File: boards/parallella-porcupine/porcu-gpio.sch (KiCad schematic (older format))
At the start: 4 parts, among them J1 CONN\\HDR\\P1\\1R02, J2 CONN\\HDR\\P1\\1R02, J3 CONN\\HDR\\P1\\2R15\\SHD, J4 CONN\\HDR\\P1\\2R15\\SHD

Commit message: Schematic is stable, PCB mostly routed.
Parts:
- removed J3, J4: CONN\\HDR\\P1\\2R15\\SHD, CONN_HDR_P1_2R15_SHD, symbol CONN\HDR\P1\2R15\SHD
- added J3: CONN\\HDR\\P1FRA\\2R06, CONN_HDR_P1FRA_2R06, symbol CONN\HDR\P1FRA\2R06
- added J4, J5: CONN\\HDR\\P1\\2R15, CONN_HDR_P1_2R15, symbol CONN\HDR\P1\2R15
- added R1, R2, R3, R4, R5, R6, R7, R8: 200, R_0805_HS, symbol R\SMD0805\1PCT\200
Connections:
- net labels added: 3P3V, PMOD11, PMOD12, PMOD13, PMOD14, PMOD21, PMOD22, PMOD23, PMOD24
- wire segments 70 -> 92
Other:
- note added: "1 -- 6"
- note added: "11\n1\n\n7\n12"
- note added: "1\n6\n\n12\n2"
- note added: "3\n5\n\n11\n4"
- note added: "5\n4\n\n10\n6"
- note added: "7 -- 12"
- note added: "7\n3\n\n9\n8"
- note added: "9\n2\n\n8\n10"
- note added: "NOTE: Pin numbering for PMODs is \nnon-standard. The numbering \nlooking into the host (female) connector:"
- note added: "PMOD Connector"
- note added: "Place series Rs to minimize\nstubs on differential GPIO_P/N."
- note added: "STD\nPMOD\n\nPMOD\nSTD"
- moved on the sheet: J1, J2

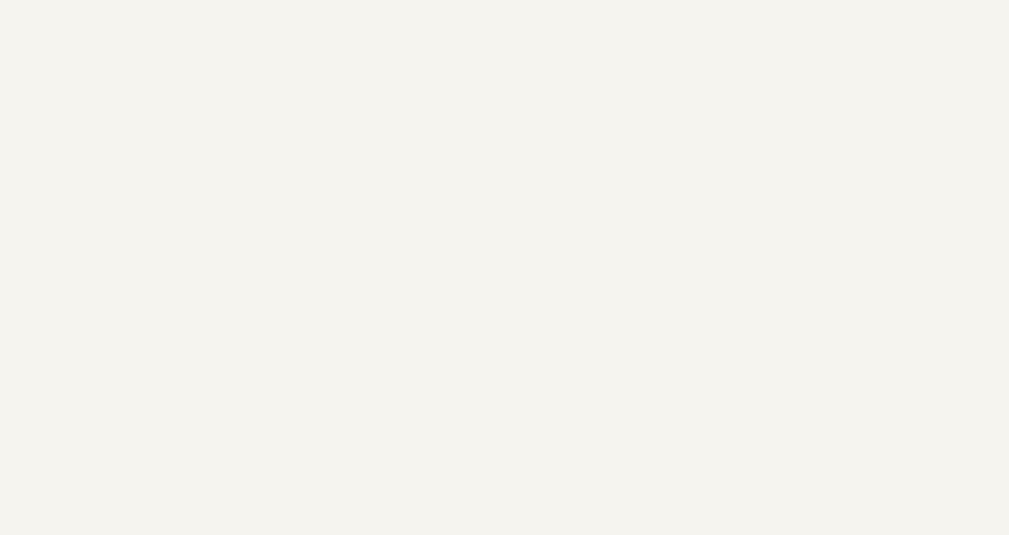
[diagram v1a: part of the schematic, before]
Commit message: Completed design w/3-row XID/YID and various 4-pin IO connectors. Fixed page ordering, changed "Mfr" field to "Manufacturer" Will now re-do to combine all misc. functions onto a single 2xN connector.
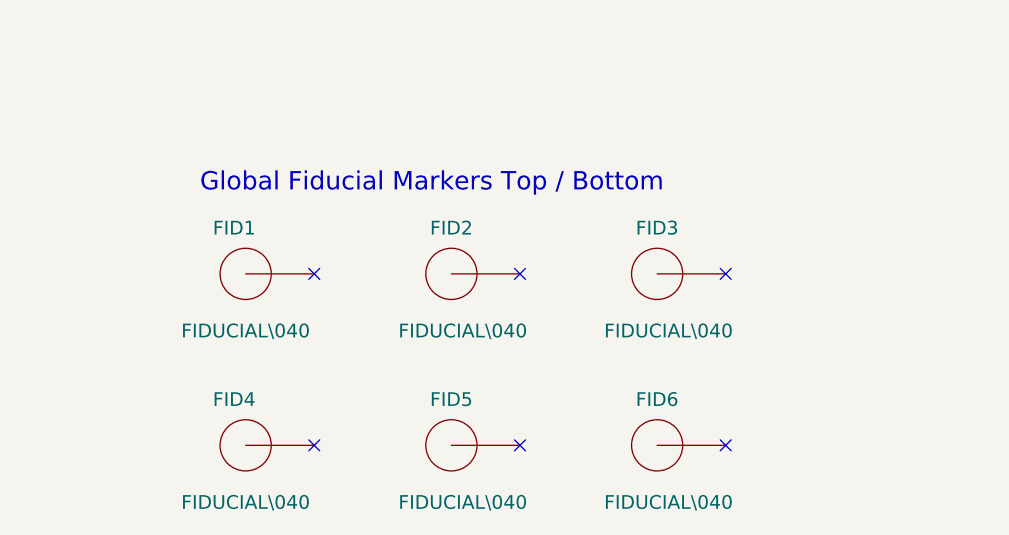
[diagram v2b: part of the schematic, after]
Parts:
- added FID1, FID2, FID3, FID4, FID5, FID6: FIDUCIAL\\040, FIDUCIAL_040, symbol FIDUCIAL\040
- J1, J2: MFR 3M -> (none); Manufacturer (none) -> 3M
- J3, J4, J5: MFR Sullins -> (none); Manufacturer (none) -> Sullins
- R1, R2, R3, R4, R5, R6, R7, R8: MFR Yageo -> (none); Manufacturer (none) -> Yageo
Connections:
- no-connect marks 0 -> 6
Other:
- note added: "Global Fiducial Markers Top / Bottom"
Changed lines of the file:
@@
 $Descr B 17000 11000
 encoding utf-8
-Sheet 6 10
+Sheet 8 10
 Title "Parallella Breakout Daughtercard"
 Date "09 May 2014"
@@
 GPIO_P23
 $Comp
-L GND #PWR010
+L GND #PWR021
 U 1 1 538C694D
 P 9250 4750
-F 0 "#PWR010" H 9250 4750 30  0001 C CNN
+F 0 "#PWR021" H 9250 4750 30  0001 C CNN
 F 1 "GND" H 9250 4680 30  0001 C CNN
 F 2 "" H 9250 4750 60  0000 C CNN
@@
 $EndComp
 $Comp
-L GND #PWR011
+L GND #PWR022
 U 1 1 538C6961
 P 11550 4750
-F 0 "#PWR011" H 11550 4750 30  0001 C CNN
+F 0 "#PWR022" H 11550 4750 30  0001 C CNN
 F 1 "GND" H 11550 4680 30  0001 C CNN
 F 2 "" H 11550 4750 60  0000 C CNN
@@
 $EndComp
 $Comp
-L GND #PWR012
+L GND #PWR023
 U 1 1 538C6975
 P 9250 7700
-F 0 "#PWR012" H 9250 7700 30  0001 C CNN
+F 0 "#PWR023" H 9250 7700 30  0001 C CNN
 F 1 "GND" H 9250 7630 30  0001 C CNN
 F 2 "" H 9250 7700 60  0000 C CNN
@@
 $EndComp
 $Comp
-L GND #PWR013
+L GND #PWR024
 U 1 1 538C6989
 P 11550 7650
-F 0 "#PWR013" H 11550 7650 30  0001 C CNN
+F 0 "#PWR024" H 11550 7650 30  0001 C CNN
 F 1 "GND" H 11550 7580 30  0001 C CNN
 F 2 "" H 11550 7650 60  0000 C CNN
@@
 GPIO_P[0..23]
 $Comp
-L GND #PWR014
+L GND #PWR025
 U 1 1 538C747F
 P 5600 3100
-F 0 "#PWR014" H 5600 3100 30  0001 C CNN
+F 0 "#PWR025" H 5600 3100 30  0001 C CNN
 F 1 "GND" H 5600 3030 30  0001 C CNN
 F 2 "" H 5600 3100 60  0000 C CNN
@@
 F 3 "" H 5050 2750 60  0001 C CNN
 F 4 "961102-6404-AR" H 5200 2700 50  0000 C CNN "MFRPN"
-F 5 "3M" H 5050 2900 50  0001 C CNN "MFR"
+F 5 "3M" H 5050 2900 50  0001 C CNN "Manufacturer"
 	1    5050 2550
 	1    0    0    -1
@@
 F 3 "" H 5050 3150 60  0001 C CNN
 F 4 "961102-6404-AR" H 5200 3100 50  0000 C CNN "MFRPN"
-F 5 "3M" H 5050 3300 50  0001 C CNN "MFR"
+F 5 "3M" H 5050 3300 50  0001 C CNN "Manufacturer"
 	1    5050 2950
 	1    0    0    -1
@@
 F 3 "" V 6330 5500 30  0000 C CNN
 F 4 "RC0805FR-07200RL" V 6340 5520 60  0001 C CNN "MFRPN"
-F 5 "Yageo" V 6450 5500 60  0001 C CNN "MFR"
+F 5 "Yageo" V 6450 5500 60  0001 C CNN "Manufacturer"
 	1    6250 5500
 	0    -1   -1   0
@@
 F 3 "" H 5050 5800 60  0001 C CNN
 F 4 "PPPC062LJBN-RC" H 5200 5750 50  0000 C CNN "MFRPN"
-F 5 "Sullins" H 5100 5950 50  0001 C CNN "MFR"
+F 5 "Sullins" H 5100 5950 50  0001 C CNN "Manufacturer"
 	1    5100 5350
 	1    0    0    -1
 $EndComp
 $Comp
-L GND #PWR015
+L GND #PWR026
 U 1 1 5397567C
 P 4700 5750
-F 0 "#PWR015" H 4700 5750 30  0001 C CNN
+F 0 "#PWR026" H 4700 5750 30  0001 C CNN
 F 1 "GND" H 4700 5680 30  0001 C CNN
 F 2 "" H 4700 5750 60  0000 C CNN
@@
 $EndComp
 $Comp
-L GND #PWR016
+L GND #PWR027
 U 1 1 53975690
 P 5500 5750
-F 0 "#PWR016" H 5500 5750 30  0001 C CNN
+F 0 "#PWR027" H 5500 5750 30  0001 C CNN
 F 1 "GND" H 5500 5680 30  0001 C CNN
 F 2 "" H 5500 5750 60  0000 C CNN
@@
 F 3 "" V 6330 5600 30  0000 C CNN
 F 4 "RC0805FR-07200RL" V 6100 5500 60  0000 C CNN "MFRPN"
-F 5 "Yageo" V 6450 5600 60  0001 C CNN "MFR"
+F 5 "Yageo" V 6450 5600 60  0001 C CNN "Manufacturer"
 	1    6250 5600
 	0    -1   -1   0
@@
 F 3 "" H 10400 4950 60  0001 C CNN
 F 4 "PRPC015DAAN-RC" H 10550 4900 50  0000 C CNN "MFRPN"
-F 5 "Sullins" H 10400 5100 50  0001 C CNN "MFR"
+F 5 "Sullins" H 10400 5100 50  0001 C CNN "Manufacturer"
 	1    10400 4050
 	1    0    0    -1
@@
 F 3 "" H 10400 7850 60  0001 C CNN
 F 4 "PRPC015DAAN-RC" H 10550 7800 50  0000 C CNN "MFRPN"
-F 5 "Sullins" H 10400 8000 50  0001 C CNN "MFR"
+F 5 "Sullins" H 10400 8000 50  0001 C CNN "Manufacturer"
 	1    10400 6950
 	1    0    0    -1
@@
 F 3 "" V 6330 5400 30  0000 C CNN
 F 4 "RC0805FR-07200RL" V 6340 5420 60  0001 C CNN "MFRPN"
-F 5 "Yageo" V 6450 5400 60  0001 C CNN "MFR"
+F 5 "Yageo" V 6450 5400 60  0001 C CNN "Manufacturer"
 	1    6250 5400
 	0    -1   -1   0
@@
 F 3 "" V 6330 5300 30  0000 C CNN
 F 4 "RC0805FR-07200RL" V 6340 5320 60  0001 C CNN "MFRPN"
-F 5 "Yageo" V 6450 5300 60  0001 C CNN "MFR"
+F 5 "Yageo" V 6450 5300 60  0001 C CNN "Manufacturer"
 	1    6250 5300
 	0    -1   -1   0
@@
 F 3 "" V 4030 5500 30  0000 C CNN
 F 4 "RC0805FR-07200RL" V 4040 5520 60  0001 C CNN "MFRPN"
-F 5 "Yageo" V 4150 5500 60  0001 C CNN "MFR"
+F 5 "Yageo" V 4150 5500 60  0001 C CNN "Manufacturer"
 	1    3950 5500
 	0    -1   -1   0
@@
 F 3 "" V 4030 5600 30  0000 C CNN
 F 4 "RC0805FR-07200RL" V 3800 5500 60  0001 C CNN "MFRPN"
-F 5 "Yageo" V 4150 5600 60  0001 C CNN "MFR"
+F 5 "Yageo" V 4150 5600 60  0001 C CNN "Manufacturer"
 	1    3950 5600
 	0    -1   -1   0
@@
 F 3 "" V 4030 5400 30  0000 C CNN
 F 4 "RC0805FR-07200RL" V 4040 5420 60  0001 C CNN "MFRPN"
-F 5 "Yageo" V 4150 5400 60  0001 C CNN "MFR"
+F 5 "Yageo" V 4150 5400 60  0001 C CNN "Manufacturer"
 	1    3950 5400
 	0    -1   -1   0
@@
 F 3 "" V 4030 5300 30  0000 C CNN
 F 4 "RC0805FR-07200RL" V 4040 5320 60  0001 C CNN "MFRPN"
-F 5 "Yageo" V 4150 5300 60  0001 C CNN "MFR"
+F 5 "Yageo" V 4150 5300 60  0001 C CNN "Manufacturer"
 	1    3950 5300
 	0    -1   -1   0
 $EndComp
+$Comp
+L FIDUCIAL\040 FID1
+U 1 1 539F4400
+P 7850 9050
+F 0 "FID1" H 7800 9250 60  0000 C CNN
+F 1 "FIDUCIAL\\040" H 7850 8800 60  0000 C CNN
+F 2 "FIDUCIAL_040" H 7850 9800 60  0001 C CNN
+F 3 "N/A" H 7850 9450 60  0001 C CNN
+F 4 "N/A" H 7850 9700 80  0001 C CNN "MFRPN"
+F 5 "N/A" H 7850 9550 60  0001 C CNN "Manufacturer"
+	1    7850 9050
+	1    0    0    -1
+$EndComp
+$Comp
+L FIDUCIAL\040 FID2
+U 1 1 539F4422
+P 8750 9050
+F 0 "FID2" H 8750 9250 60  0000 C CNN
+F 1 "FIDUCIAL\\040" H 8800 8800 60  0000 C CNN
+F 2 "FIDUCIAL_040" H 8750 9800 60  0001 C CNN
+F 3 "N/A" H 8750 9450 60  0001 C CNN
+F 4 "N/A" H 8750 9700 80  0001 C CNN "MFRPN"
+F 5 "N/A" H 8750 9550 60  0001 C CNN "Manufacturer"
+	1    8750 9050
+	1    0    0    -1
+$EndComp
+$Comp
+L FIDUCIAL\040 FID3
+U 1 1 539F4444
+P 9650 9050
+F 0 "FID3" H 9650 9250 60  0000 C CNN
+F 1 "FIDUCIAL\\040" H 9700 8800 60  0000 C CNN
+F 2 "FIDUCIAL_040" H 9650 9800 60  0001 C CNN
+F 3 "N/A" H 9650 9450 60  0001 C CNN
+F 4 "N/A" H 9650 9700 80  0001 C CNN "MFRPN"
+F 5 "N/A" H 9650 9550 60  0001 C CNN "Manufacturer"
+	1    9650 9050
+	1    0    0    -1
+$EndComp
+Text Notes 7650 8700 0    80   ~ 0
+Global Fiducial Markers Top / Bottom
+NoConn ~ 8150 9050
+NoConn ~ 9050 9050
+NoConn ~ 9950 9050
+$Comp
+L FIDUCIAL\040 FID4
+U 1 1 539F4E47
+P 7850 9800
+F 0 "FID4" H 7800 10000 60  0000 C CNN
+F 1 "FIDUCIAL\\040" H 7850 9550 60  0000 C CNN
+F 2 "FIDUCIAL_040" H 7850 10550 60  0001 C CNN
+F 3 "N/A" H 7850 10200 60  0001 C CNN
+F 4 "N/A" H 7850 10450 80  0001 C CNN "MFRPN"
+F 5 "N/A" H 7850 10300 60  0001 C CNN "Manufacturer"
+	1    7850 9800
+	1    0    0    -1
+$EndComp
+$Comp
+L FIDUCIAL\040 FID5
+U 1 1 539F4E4F
+P 8750 9800
+F 0 "FID5" H 8750 10000 60  0000 C CNN
+F 1 "FIDUCIAL\\040" H 8800 9550 60  0000 C CNN
+F 2 "FIDUCIAL_040" H 8750 10550 60  0001 C CNN
+F 3 "N/A" H 8750 10200 60  0001 C CNN
+F 4 "N/A" H 8750 10450 80  0001 C CNN "MFRPN"
+F 5 "N/A" H 8750 10300 60  0001 C CNN "Manufacturer"
+	1    8750 9800
+	1    0    0    -1
+$EndComp
+$Comp
+L FIDUCIAL\040 FID6
+U 1 1 539F4E57
+P 9650 9800
+F 0 "FID6" H 9650 10000 60  0000 C CNN
+F 1 "FIDUCIAL\\040" H 9700 9550 60  0000 C CNN
+F 2 "FIDUCIAL_040" H 9650 10550 60  0001 C CNN
+F 3 "N/A" H 9650 10200 60  0001 C CNN
+F 4 "N/A" H 9650 10450 80  0001 C CNN "MFRPN"
+F 5 "N/A" H 9650 10300 60  0001 C CNN "Manufacturer"
+	1    9650 9800
+	1    0    0    -1
+$EndComp
+NoConn ~ 8150 9800
+NoConn ~ 9050 9800
+NoConn ~ 9950 9800
 $EndSCHEMATC

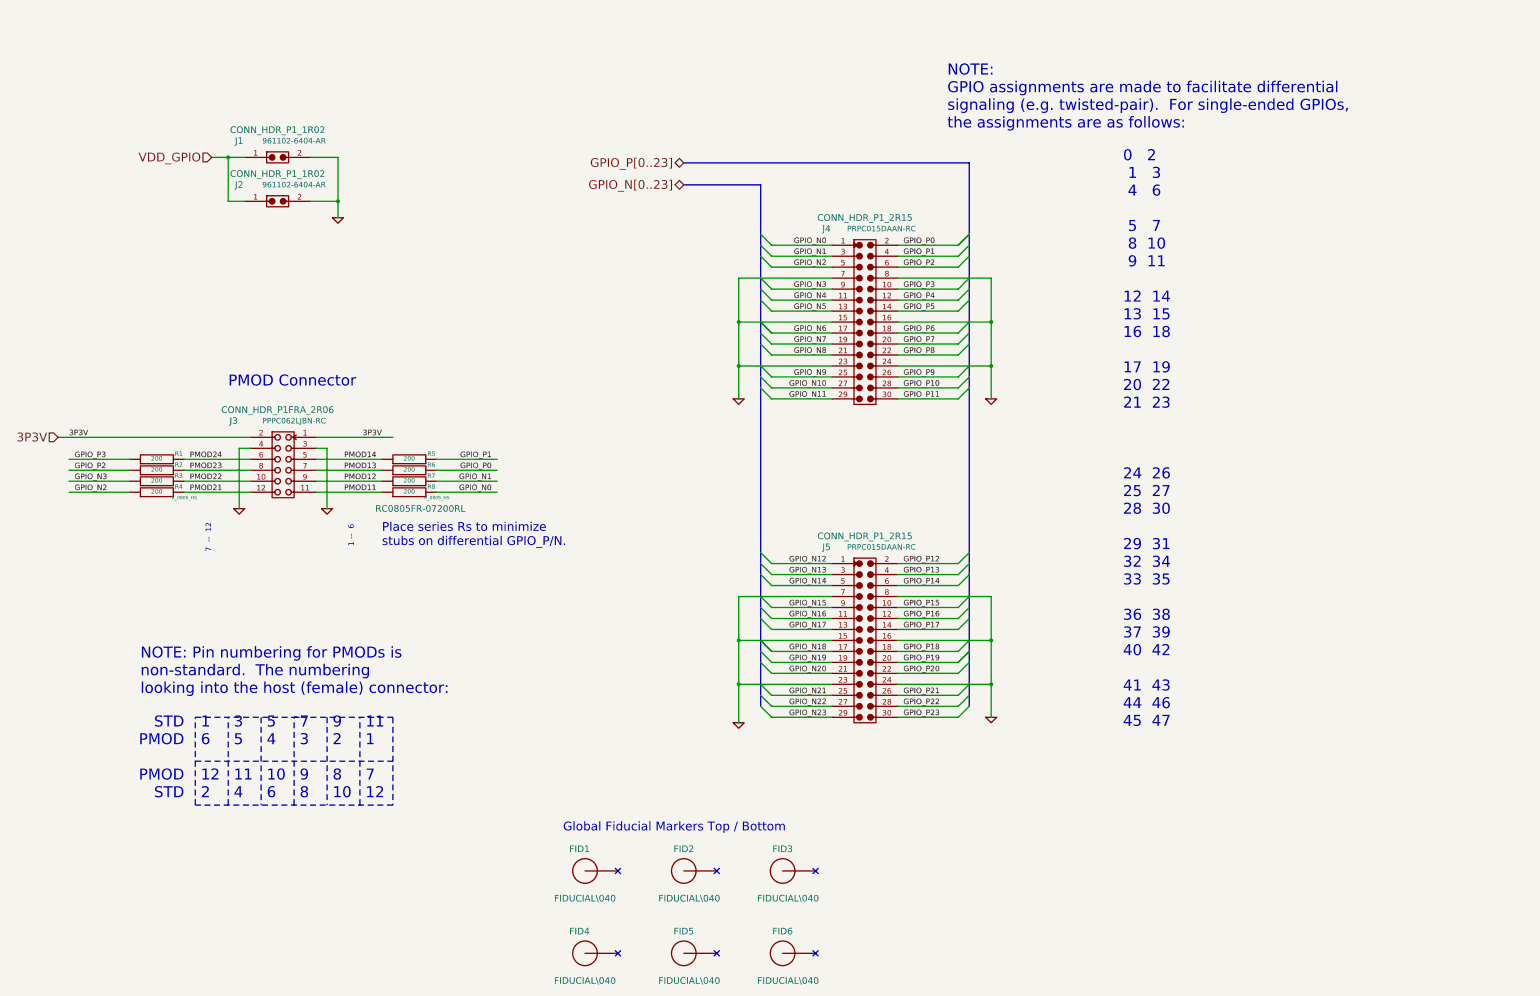
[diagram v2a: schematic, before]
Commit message: Changed to a single header for all the PEC_POWER/misc. stuff. Added 3D models for shrouded & right-angle connectors.
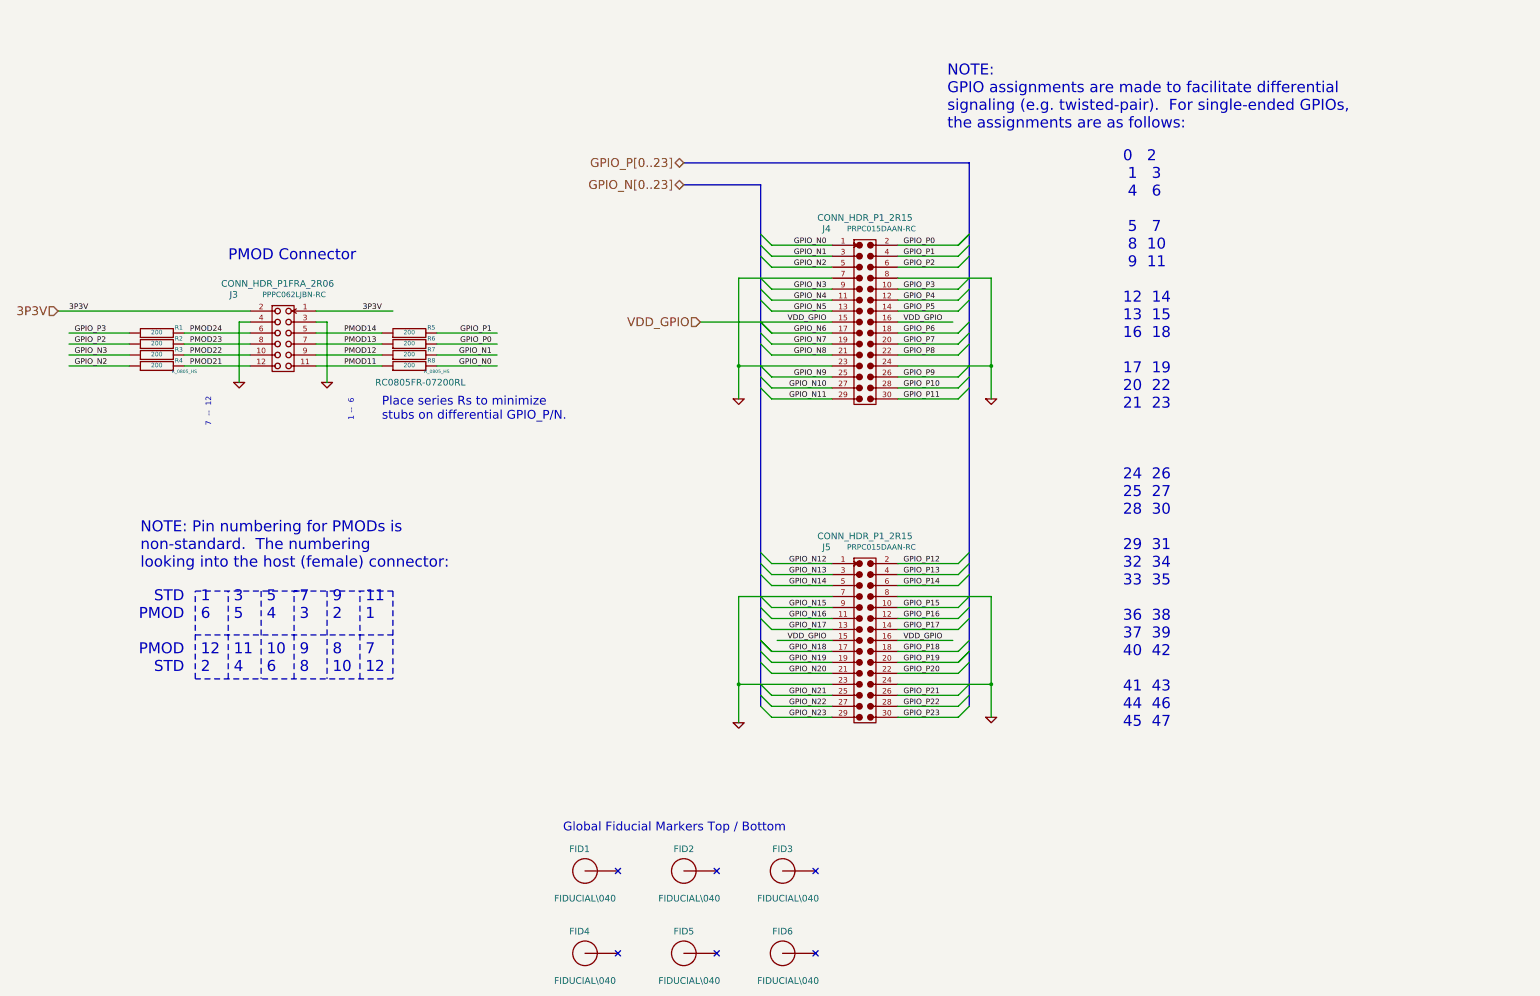
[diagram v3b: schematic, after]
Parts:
- removed J1, J2: CONN\\HDR\\P1\\1R02, CONN_HDR_P1_1R02, symbol CONN\HDR\P1\1R02
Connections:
- wire segments 92 -> 86
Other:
- moved on the sheet: J3, R1, R2, R3, R4, R5, R6, R7, R8

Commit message: Ready for full review.
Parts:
- renumbered FID4 to FID2, FID2 to FID3, FID5 to FID4, FID3 to FID5, J3 to J5, J4 to J6, J5 to J7
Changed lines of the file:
@@
 Sheet 8 10
 Title "Parallella Breakout Daughtercard"
-Date "09 May 2014"
+Date "19 Jun 2014"
 Rev "*"
 Comp "Adapteva, Inc., 1666 Massachusetts Ave., Lexington, MA, 02420"
@@
 GPIO_P23
 $Comp
-L GND #PWR018
+L GND #PWR017
 U 1 1 538C694D
 P 9250 4750
-F 0 "#PWR018" H 9250 4750 30  0001 C CNN
+F 0 "#PWR017" H 9250 4750 30  0001 C CNN
 F 1 "GND" H 9250 4680 30  0001 C CNN
 F 2 "" H 9250 4750 60  0000 C CNN
@@
 $EndComp
 $Comp
-L GND #PWR019
+L GND #PWR018
 U 1 1 538C6961
 P 11550 4750
-F 0 "#PWR019" H 11550 4750 30  0001 C CNN
+F 0 "#PWR018" H 11550 4750 30  0001 C CNN
 F 1 "GND" H 11550 4680 30  0001 C CNN
 F 2 "" H 11550 4750 60  0000 C CNN
@@
 $EndComp
 $Comp
-L GND #PWR020
+L GND #PWR019
 U 1 1 538C6975
 P 9250 7700
-F 0 "#PWR020" H 9250 7700 30  0001 C CNN
+F 0 "#PWR019" H 9250 7700 30  0001 C CNN
 F 1 "GND" H 9250 7630 30  0001 C CNN
 F 2 "" H 9250 7700 60  0000 C CNN
@@
 $EndComp
 $Comp
-L GND #PWR021
+L GND #PWR020
 U 1 1 538C6989
 P 11550 7650
-F 0 "#PWR021" H 11550 7650 30  0001 C CNN
+F 0 "#PWR020" H 11550 7650 30  0001 C CNN
 F 1 "GND" H 11550 7580 30  0001 C CNN
 F 2 "" H 11550 7650 60  0000 C CNN
@@
 3P3V
 $Comp
-L CONN\HDR\P1FRA\2R06 J3
+L CONN\HDR\P1FRA\2R06 J5
 U 1 1 53975602
 P 5100 4200
-F 0 "J3" H 4650 4600 60  0000 C CNN
+F 0 "J5" H 4650 4600 60  0000 C CNN
 F 1 "CONN\\HDR\\P1FRA\\2R06" H 5000 4900 60  0001 C CNN
 F 2 "CONN_HDR_P1FRA_2R06" H 5050 4700 60  0000 C CNN
@@
 $EndComp
 $Comp
-L GND #PWR022
+L GND #PWR021
 U 1 1 5397567C
 P 4700 4600
-F 0 "#PWR022" H 4700 4600 30  0001 C CNN
+F 0 "#PWR021" H 4700 4600 30  0001 C CNN
 F 1 "GND" H 4700 4530 30  0001 C CNN
 F 2 "" H 4700 4600 60  0000 C CNN
@@
 $EndComp
 $Comp
-L GND #PWR023
+L GND #PWR022
 U 1 1 53975690
 P 5500 4600
-F 0 "#PWR023" H 5500 4600 30  0001 C CNN
+F 0 "#PWR022" H 5500 4600 30  0001 C CNN
 F 1 "GND" H 5500 4530 30  0001 C CNN
 F 2 "" H 5500 4600 60  0000 C CNN
@@
 Place series Rs to minimize\nstubs on differential GPIO_P/N.
 $Comp
-L CONN\HDR\P1\2R15 J4
+L CONN\HDR\P1\2R15 J6
 U 1 1 539792C9
 P 10400 4050
-F 0 "J4" H 10050 4900 60  0000 C CNN
+F 0 "J6" H 10050 4900 60  0000 C CNN
 F 1 "CONN\\HDR\\P1\\2R15" H 10400 5200 60  0001 C CNN
 F 2 "CONN_HDR_P1_2R15" H 10400 5000 60  0000 C CNN
@@
 $EndComp
 $Comp
-L CONN\HDR\P1\2R15 J5
+L CONN\HDR\P1\2R15 J7
 U 1 1 539792F9
 P 10400 6950
-F 0 "J5" H 10050 7800 60  0000 C CNN
+F 0 "J7" H 10050 7800 60  0000 C CNN
 F 1 "CONN\\HDR\\P1\\2R15" H 10400 8100 60  0001 C CNN
 F 2 "CONN_HDR_P1_2R15" H 10400 7900 60  0000 C CNN
@@
 $EndComp
 $Comp
-L FIDUCIAL\040 FID2
+L FIDUCIAL\040 FID3
 U 1 1 539F4422
 P 8750 9050
-F 0 "FID2" H 8750 9250 60  0000 C CNN
+F 0 "FID3" H 8750 9250 60  0000 C CNN
 F 1 "FIDUCIAL\\040" H 8800 8800 60  0000 C CNN
 F 2 "FIDUCIAL_040" H 8750 9800 60  0001 C CNN
@@
 $EndComp
 $Comp
-L FIDUCIAL\040 FID3
+L FIDUCIAL\040 FID5
 U 1 1 539F4444
 P 9650 9050
-F 0 "FID3" H 9650 9250 60  0000 C CNN
+F 0 "FID5" H 9650 9250 60  0000 C CNN
 F 1 "FIDUCIAL\\040" H 9700 8800 60  0000 C CNN
 F 2 "FIDUCIAL_040" H 9650 9800 60  0001 C CNN
@@
 NoConn ~ 9950 9050
 $Comp
-L FIDUCIAL\040 FID4
+L FIDUCIAL\040 FID2
 U 1 1 539F4E47
 P 7850 9800
-F 0 "FID4" H 7800 10000 60  0000 C CNN
+F 0 "FID2" H 7800 10000 60  0000 C CNN
 F 1 "FIDUCIAL\\040" H 7850 9550 60  0000 C CNN
 F 2 "FIDUCIAL_040" H 7850 10550 60  0001 C CNN
@@
 $EndComp
 $Comp
-L FIDUCIAL\040 FID5
+L FIDUCIAL\040 FID4
 U 1 1 539F4E4F
 P 8750 9800
-F 0 "FID5" H 8750 10000 60  0000 C CNN
+F 0 "FID4" H 8750 10000 60  0000 C CNN
 F 1 "FIDUCIAL\\040" H 8800 9550 60  0000 C CNN
 F 2 "FIDUCIAL_040" H 8750 10550 60  0001 C CNN
